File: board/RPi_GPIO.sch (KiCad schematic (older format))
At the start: 29 parts, among them IC1 ATMEGA328P-P, IC2 RFM69HW, J1 RPi_GPIO, P1 FTDI_CONN_01X06, P2 BATT_IN, P3 V_SRC_JPR, P4 UART_SRC_JPR, P5 LED_CONN, P6 SW_CONN, P7 CONN_01X01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

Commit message: first draft of the HAT layout
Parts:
- C1: footprint (none) -> Capacitors_SMD:c_elec_4x4.5
- C2, C5, C6: footprint (none) -> Capacitors_SMD:C_0805_HandSoldering
- C3, C4: footprint (none) -> Capacitors_SMD:C_1206_HandSoldering
- C7, C8: footprint (none) -> Capacitors_SMD:C_0603_HandSoldering
- D1: footprint (none) -> LEDs:LED-1206
- I1: footprint (none) -> TO_SOT_Packages_SMD:SOT-223
- IC1: footprint DIL28 -> Housings_DIP:DIP-28_W7.62mm
- IC2: footprint (none) -> mysensors-kicad:RFM69HW_SMD_Handsoldering
- JPR1, P5, P6: footprint (none) -> Pin_Headers:Pin_Header_Straight_1x02
- P1: footprint (none) -> Pin_Headers:Pin_Header_Straight_1x06
- P2: footprint (none) -> Pin_Headers:Pin_Header_Angled_1x02
- P3: footprint (none) -> Pin_Headers:Pin_Header_Straight_1x03
- P4: footprint (none) -> Pin_Headers:Pin_Header_Straight_2x03
- P7: footprint (none) -> Pin_Headers:Pin_Header_Straight_1x01
- Q1: footprint (none) -> TO_SOT_Packages_SMD:SOT-23_Handsoldering
- R1, R2, R4, R5: footprint (none) -> Resistors_SMD:R_0805_HandSoldering
- R3: footprint (none) -> Resistors_SMD:R_0603_HandSoldering
- SW1: footprint (none) -> Buttons_Switches_ThroughHole:SW_PUSH
- Y1: footprint (none) -> Crystals_Oscillators_SMD:Q_49U3HMS
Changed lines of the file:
@@
 F 0 "P2" H 6100 2900 50  0000 C CNN
 F 1 "BATT_IN" V 6200 2750 50  0000 C CNN
-F 2 "" H 6100 2750 60  0000 C CNN
+F 2 "Pin_Headers:Pin_Header_Angled_1x02" H 6100 2750 60  0001 C CNN
 F 3 "" H 6100 2750 60  0000 C CNN
 	1    6100 2750
@@
 F 0 "IC1" H 1500 6950 40  0000 L BNN
 F 1 "ATMEGA328P-P" H 2650 4300 40  0000 L BNN
-F 2 "DIL28" H 2250 5700 30  0000 C CIN
+F 2 "Housings_DIP:DIP-28_W7.62mm" H 2250 5700 30  0000 C CIN
 F 3 "" H 2250 5700 60  0000 C CNN
 	1    2250 5700
@@
 F 0 "C5" V 3600 5900 50  0000 L CNN
 F 1 "0.1µF" V 3800 5950 50  0000 C CNN
-F 2 "" H 3700 5950 60  0000 C CNN
+F 2 "Capacitors_SMD:C_0805_HandSoldering" H 3700 5950 60  0001 C CNN
 F 3 "" H 3700 5950 60  0000 C CNN
 	1    3700 5950
@@
 F 0 "C6" H 1175 6350 50  0000 L CNN
 F 1 "0.1µF" H 1175 6150 50  0000 L CNN
-F 2 "" H 1188 6100 30  0000 C CNN
+F 2 "Capacitors_SMD:C_0805_HandSoldering" H 1188 6100 30  0001 C CNN
 F 3 "" H 1150 6250 60  0000 C CNN
 	1    1150 6250
@@
 F 0 "R1" H 7630 1470 50  0000 L CNN
 F 1 "10K" H 7630 1410 50  0000 L CNN
-F 2 "" H 7600 1450 60  0000 C CNN
+F 2 "Resistors_SMD:R_0805_HandSoldering" H 7600 1450 60  0001 C CNN
 F 3 "" H 7600 1450 60  0000 C CNN
 	1    7600 1450
@@
 F 0 "R2" H 8330 1470 50  0000 L CNN
 F 1 "10K" H 8330 1410 50  0000 L CNN
-F 2 "" H 8300 1450 60  0000 C CNN
+F 2 "Resistors_SMD:R_0805_HandSoldering" H 8300 1450 60  0001 C CNN
 F 3 "" H 8300 1450 60  0000 C CNN
 	1    8300 1450
@@
 F 0 "Q1" V 7900 1500 50  0000 R CNN
 F 1 "BSS138_GSD" V 8250 1800 50  0000 R CNN
-F 2 "" H 8200 1650 29  0000 C CNN
+F 2 "TO_SOT_Packages_SMD:SOT-23_Handsoldering" H 8200 1650 29  0001 C CNN
 F 3 "" H 8000 1550 60  0000 C CNN
 	1    8000 1550
@@
 F 0 "P3" V 10050 1500 50  0000 C CNN
 F 1 "V_SRC_JPR" V 10150 1250 50  0000 C CNN
-F 2 "" H 10050 1250 60  0000 C CNN
+F 2 "Pin_Headers:Pin_Header_Straight_1x03" H 10050 1250 60  0001 C CNN
 F 3 "" H 10050 1250 60  0000 C CNN
 	1    10050 1250
@@
 F 0 "P4" V 10050 2950 50  0000 C CNN
 F 1 "UART_SRC_JPR" H 10050 2500 50  0000 C CNN
-F 2 "" H 10050 1500 60  0000 C CNN
+F 2 "Pin_Headers:Pin_Header_Straight_2x03" H 10050 1500 60  0001 C CNN
 F 3 "" H 10050 1500 60  0000 C CNN
 	1    10050 2700
@@
 F 0 "I1" H 7400 2800 60  0000 C CNN
 F 1 "TC1108" H 7600 2350 60  0000 C CNN
-F 2 "" H 7500 2600 60  0000 C CNN
+F 2 "TO_SOT_Packages_SMD:SOT-223" H 7500 2600 60  0001 C CNN
 F 3 "" H 7500 2600 60  0000 C CNN
 	1    7600 2650
@@
 F 0 "C4" H 8160 2870 50  0000 L CNN
 F 1 "1µF" H 8160 2720 50  0000 L CNN
-F 2 "" H 8150 2800 60  0000 C CNN
+F 2 "Capacitors_SMD:C_1206_HandSoldering" H 8150 2800 60  0001 C CNN
 F 3 "" H 8150 2800 60  0000 C CNN
 	1    8150 2800
@@
 F 0 "C3" H 6810 2820 50  0000 L CNN
 F 1 "1µF" H 6810 2670 50  0000 L CNN
-F 2 "" H 6800 2750 60  0000 C CNN
+F 2 "Capacitors_SMD:C_1206_HandSoldering" H 6800 2750 60  0001 C CNN
 F 3 "" H 6800 2750 60  0000 C CNN
 	1    6800 2750
@@
 F 0 "Y1" H 4450 5250 50  0000 C CNN
 F 1 "16MHz" H 4450 5450 50  0000 C CNN
-F 2 "" H 4450 5350 60  0000 C CNN
+F 2 "Crystals_Oscillators_SMD:Q_49U3HMS" H 4450 5350 60  0001 C CNN
 F 3 "" H 4450 5350 60  0000 C CNN
 	1    4450 5350
@@
 F 0 "C7" V 4500 5150 50  0000 L CNN
 F 1 "22pF" V 4600 5150 50  0000 L CNN
-F 2 "" H 4700 5200 60  0000 C CNN
+F 2 "Capacitors_SMD:C_0603_HandSoldering" H 4700 5200 60  0001 C CNN
 F 3 "" H 4700 5200 60  0000 C CNN
 	1    4700 5200
@@
 F 0 "C8" V 4800 5450 50  0000 L CNN
 F 1 "22pF" V 4900 5400 50  0000 L CNN
-F 2 "" H 4700 5500 60  0000 C CNN
+F 2 "Capacitors_SMD:C_0603_HandSoldering" H 4700 5500 60  0001 C CNN
 F 3 "" H 4700 5500 60  0000 C CNN
 	1    4700 5500
@@
 F 0 "R5" V 3800 5600 50  0000 L CNN
 F 1 "10K" V 3600 5600 50  0000 L CNN
-F 2 "" H 3700 5650 60  0000 C CNN
+F 2 "Resistors_SMD:R_0805_HandSoldering" H 3700 5650 60  0001 C CNN
 F 3 "" H 3700 5650 60  0000 C CNN
 	1    3700 5650
@@
 F 0 "C1" H 4460 2670 50  0000 L CNN
 F 1 "10µF" H 4460 2520 50  0000 L CNN
-F 2 "" H 4450 2600 60  0000 C CNN
+F 2 "Capacitors_SMD:c_elec_4x4.5" H 4450 2600 60  0001 C CNN
 F 3 "" H 4450 2600 60  0000 C CNN
 	1    4450 2600
@@
 F 0 "C2" H 4810 2670 50  0000 L CNN
 F 1 "0.1µF" H 4810 2520 50  0000 L CNN
-F 2 "" H 4800 2600 60  0000 C CNN
+F 2 "Capacitors_SMD:C_0805_HandSoldering" H 4800 2600 60  0001 C CNN
 F 3 "" H 4800 2600 60  0000 C CNN
 	1    4800 2600
@@
 F 0 "D1" V 6800 4500 50  0000 L CNN
 F 1 "SMD_LED" V 6650 4750 50  0000 R CNN
-F 2 "" V 6750 4400 60  0000 C CNN
+F 2 "LEDs:LED-1206" V 6750 4400 60  0001 C CNN
 F 3 "" V 6750 4400 60  0000 C CNN
 	1    6750 4400
@@
 F 0 "R3" H 6600 4150 50  0000 L CNN
 F 1 "560R" H 6500 4050 50  0000 L CNN
-F 2 "" H 6750 4100 60  0000 C CNN
+F 2 "Resistors_SMD:R_0603_HandSoldering" H 6750 4100 60  0001 C CNN
 F 3 "" H 6750 4100 60  0000 C CNN
 	1    6750 4100
@@
 F 0 "P5" H 7300 3850 50  0000 C CNN
 F 1 "LED_CONN" V 7400 3700 50  0000 C CNN
-F 2 "" H 7300 3700 60  0000 C CNN
+F 2 "Pin_Headers:Pin_Header_Straight_1x02" H 7300 3700 60  0001 C CNN
 F 3 "" H 7300 3700 60  0000 C CNN
 	1    7300 3700
@@
 F 0 "P1" H 6050 1750 50  0000 C CNN
 F 1 "FTDI_CONN_01X06" V 6250 1400 50  0000 C CNN
-F 2 "" H 6050 1400 60  0000 C CNN
+F 2 "Pin_Headers:Pin_Header_Straight_1x06" H 6050 1400 60  0001 C CNN
 F 3 "" H 6050 1400 60  0000 C CNN
 	1    6050 1400
@@
 F 0 "P6" H 7250 6000 50  0000 C CNN
 F 1 "SW_CONN" V 7350 5850 50  0000 C CNN
-F 2 "" H 7250 5850 60  0000 C CNN
+F 2 "Pin_Headers:Pin_Header_Straight_1x02" H 7250 5850 60  0001 C CNN
 F 3 "" H 7250 5850 60  0000 C CNN
 	1    7250 5850
@@
 F 0 "R4" H 6480 5620 50  0000 L CNN
 F 1 "10K" H 6480 5560 50  0000 L CNN
-F 2 "" H 6450 5600 60  0000 C CNN
+F 2 "Resistors_SMD:R_0805_HandSoldering" H 6450 5600 60  0001 C CNN
 F 3 "" H 6450 5600 60  0000 C CNN
 	1    6450 5600
@@
 F 0 "SW1" H 6600 5900 30  0000 C CNN
 F 1 "SWITCH" H 6600 5850 30  0000 C CNN
-F 2 "" H 6750 5900 60  0000 C CNN
+F 2 "Buttons_Switches_ThroughHole:SW_PUSH" H 6750 5900 60  0001 C CNN
 F 3 "" H 6750 5900 60  0000 C CNN
 	1    6750 5900
@@
 F 0 "IC2" H 9050 4700 60  0000 C CNN
 F 1 "RFM69HW" H 9500 3350 60  0000 C CNN
-F 2 "" H 9350 4550 60  0000 C CNN
+F 2 "mysensors-kicad:RFM69HW_SMD_Handsoldering" H 9350 4550 60  0001 C CNN
 F 3 "" H 9350 4550 60  0000 C CNN
 	1    9350 4550
@@
 F 0 "P7" H 10450 5550 50  0000 C CNN
 F 1 "CONN_01X01" V 10550 5450 50  0000 C CNN
-F 2 "" H 10450 5450 60  0000 C CNN
+F 2 "Pin_Headers:Pin_Header_Straight_1x01" H 10450 5450 60  0001 C CNN
 F 3 "" H 10450 5450 60  0000 C CNN
 	1    10450 5450
@@
 F 0 "JPR1" H 6750 3850 50  0000 C CNN
 F 1 "NC_JPR" H 6800 3950 50  0000 C CNN
-F 2 "" H 6550 3850 60  0000 C CNN
+F 2 "Pin_Headers:Pin_Header_Straight_1x02" H 6550 3850 60  0001 C CNN
 F 3 "" H 6550 3850 60  0000 C CNN
 	1    6550 3850

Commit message: changed LED resistor to 75ohms (0603 package)
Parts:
- R3: value 560R -> 75R
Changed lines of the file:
@@
 P 6750 4100
 F 0 "R3" H 6600 4150 50  0000 L CNN
-F 1 "560R" H 6500 4050 50  0000 L CNN
+F 1 "75R" H 6550 4050 50  0000 L CNN
 F 2 "Resistors_SMD:R_0603_HandSoldering" H 6750 4100 60  0001 C CNN
 F 3 "" H 6750 4100 60  0000 C CNN

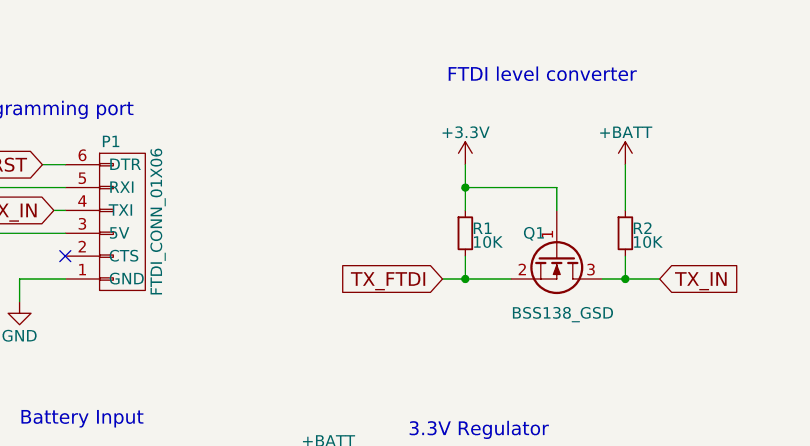
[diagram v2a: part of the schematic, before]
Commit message: fixed 3.3v error, and button rotation bug
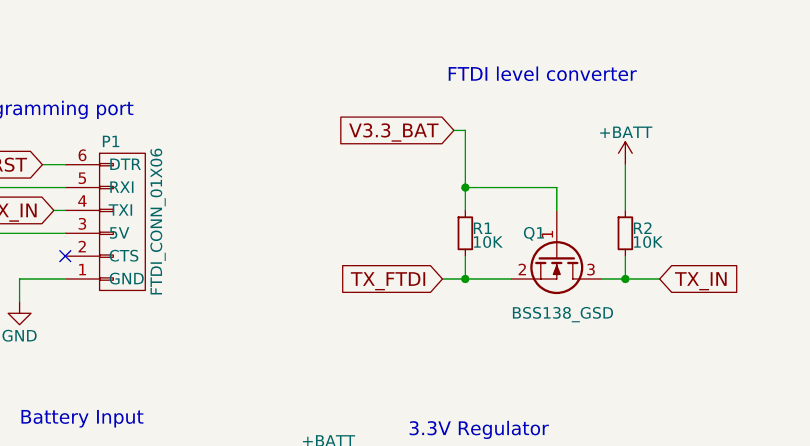
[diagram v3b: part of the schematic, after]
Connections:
- wire segments 146 -> 147
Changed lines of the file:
@@
 LIBS:contrib
 LIBS:valves
-LIBS:RPi_Hat-cache
 EELAYER 25 0
 EELAYER END
@@
 	1    0    0    -1
 $EndComp
-$Comp
-L +3.3V #PWR010
-U 1 1 560D442F
-P 7600 1150
-F 0 "#PWR010" H 7600 1000 50  0001 C CNN
-F 1 "+3.3V" H 7600 1290 50  0000 C CNN
-F 2 "" H 7600 1150 60  0000 C CNN
-F 3 "" H 7600 1150 60  0000 C CNN
-	1    7600 1150
-	1    0    0    -1
-$EndComp
 Text GLabel 7500 1650 0    60   Input ~ 0
 TX_FTDI
@@
 $EndComp
 $Comp
-L GND #PWR011
+L GND #PWR010
 U 1 1 560D5F6B
 P 7000 3000
-F 0 "#PWR011" H 7000 2750 50  0001 C CNN
+F 0 "#PWR010" H 7000 2750 50  0001 C CNN
 F 1 "GND" H 7000 2850 50  0000 C CNN
 F 2 "" H 7000 3000 60  0000 C CNN
@@
 $EndComp
 $Comp
-L +BATT #PWR012
+L +BATT #PWR011
 U 1 1 560D5F97
 P 7000 2500
-F 0 "#PWR012" H 7000 2350 50  0001 C CNN
+F 0 "#PWR011" H 7000 2350 50  0001 C CNN
 F 1 "+BATT" H 7000 2640 50  0000 C CNN
 F 2 "" H 7000 2500 60  0000 C CNN
@@
 V3.3_BAT
 $Comp
-L GND #PWR013
+L GND #PWR012
 U 1 1 560D60E0
 P 8150 3000
-F 0 "#PWR013" H 8150 2750 50  0001 C CNN
+F 0 "#PWR012" H 8150 2750 50  0001 C CNN
 F 1 "GND" H 8150 2850 50  0000 C CNN
 F 2 "" H 8150 3000 60  0000 C CNN
@@
 Connection ~ 8300 1650
 Wire Wire Line
-	7600 1150 7600 1350
+	7600 1000 7600 1350
 Wire Wire Line
 	7500 1650 7800 1650
@@
 Connection ~ 4450 5500
 $Comp
-L GND #PWR014
+L GND #PWR013
 U 1 1 560D7358
 P 4950 5600
-F 0 "#PWR014" H 4950 5350 50  0001 C CNN
+F 0 "#PWR013" H 4950 5350 50  0001 C CNN
 F 1 "GND" H 4950 5450 50  0000 C CNN
 F 2 "" H 4950 5600 60  0000 C CNN
@@
 V3.3
 $Comp
-L GND #PWR015
+L GND #PWR014
 U 1 1 560D8565
 P 4800 2900
-F 0 "#PWR015" H 4800 2650 50  0001 C CNN
+F 0 "#PWR014" H 4800 2650 50  0001 C CNN
 F 1 "GND" H 4800 2750 50  0000 C CNN
 F 2 "" H 4800 2900 60  0000 C CNN
@@
 $EndComp
 $Comp
-L GND #PWR016
+L GND #PWR015
 U 1 1 560DA177
 P 6750 4700
-F 0 "#PWR016" H 6750 4450 50  0001 C CNN
+F 0 "#PWR015" H 6750 4450 50  0001 C CNN
 F 1 "GND" H 6750 4550 50  0000 C CNN
 F 2 "" H 6750 4700 60  0000 C CNN
@@
 $EndComp
 $Comp
-L GND #PWR017
+L GND #PWR016
 U 1 1 560DB627
 P 7000 6050
-F 0 "#PWR017" H 7000 5800 50  0001 C CNN
+F 0 "#PWR016" H 7000 5800 50  0001 C CNN
 F 1 "GND" H 7000 5900 50  0000 C CNN
 F 2 "" H 7000 6050 60  0000 C CNN
@@
 	9850 5450 10250 5450
 $Comp
-L GND #PWR018
+L GND #PWR017
 U 1 1 560DCDCC
 P 10050 5800
-F 0 "#PWR018" H 10050 5550 50  0001 C CNN
+F 0 "#PWR017" H 10050 5550 50  0001 C CNN
 F 1 "GND" H 10050 5650 50  0000 C CNN
 F 2 "" H 10050 5800 60  0000 C CNN
@@
 Wire Wire Line
 	6750 3900 6750 4000
+Text GLabel 7550 1000 0    60   Input ~ 0
+V3.3_BAT
+Wire Wire Line
+	7600 1000 7550 1000
 $EndSCHEMATC

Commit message: Revert "up to date with remote"
This reverts commit 92056238b58dd1545c72053bc3b2b9ea0aa8e0b0.
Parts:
- removed C7, C8: 22pF, Capacitors_SMD:C_0603_HandSoldering, symbol C_Small
- removed IC1: ATMEGA328P-P, Housings_DIP:DIP-28_W7.62mm, symbol ATMEGA328P-P
- removed P4: UART_SRC_JPR, Pin_Headers:Pin_Header_Straight_2x03, symbol CONN_02X03
- removed Y1: 16MHz, Crystals_Oscillators_SMD:Q_49U3HMS, symbol Crystal_Small
- added IC1: ATMEGA328-A, local:TQFP-32_7x7mm_Pitch0.8mm, symbol ATMEGA328-A
- added P13: ICSP, local:ISCP_header, symbol CONN_02X03
- added P2: D8, local:Pin_Header_Straight_1x03, symbol CONN_01X03
- added P4: A1, local:Pin_Header_Straight_1x03, symbol CONN_01X03
- added P5: A2, local:Pin_Header_Straight_1x03, symbol CONN_01X03
- added P6: A3, local:Pin_Header_Straight_1x03, symbol CONN_01X03
- added P7: A4, local:Pin_Header_Straight_1x03, symbol CONN_01X03
- added P8: A5, local:Pin_Header_Straight_1x03, symbol CONN_01X03
- added R10, R6, R7, R8, R9: 10K, Resistors_SMD:R_0603_HandSoldering, symbol R_Small
- added SW2: RESET, local:KSEx00G_SW, symbol SW_PUSH_SMALL
- added SW3: SWITCH_4PDT, cloudmaker:SWITCH_4PDT_MFS401N, symbol SWITCH_4PDT
- added SW4: SWITCH_4DIP_SPST, local:SW_DIP_04_GULL_BINARY, symbol SWITCH_4DIP_SPST
- added Y1: RESONATOR, local:Resonator_3.2x1.3, symbol RESONATOR
- C1: footprint Capacitors_SMD:c_elec_4x4.5 -> local:c_elec_3x5.3
- D1: footprint LEDs:LED-1206 -> LEDs:LED_1206
- I1: footprint TO_SOT_Packages_SMD:SOT-223 -> TO_SOT_Packages_SMD:SOT-23_Handsoldering
- IC2: footprint mysensors-kicad:RFM69HW_SMD_Handsoldering -> local:RFM69
- J1: footprint RPi_Hat:Samtec_HLE-120-02-XXX-DV-BE-XX-XX -> cloudmaker:Samtec_HLE-120-02-XXX-DV-BE-XX-XX
- JPR1: footprint Pin_Headers:Pin_Header_Straight_1x02 -> local:NC_SMD_JPR
- P11: renamed from P2; footprint Pin_Headers:Pin_Header_Angled_1x02 -> local:bornier2
- P3: value V_SRC_JPR -> A0; footprint Pin_Headers:Pin_Header_Straight_1x03 -> local:Pin_Header_Straight_1x03
- R1, R2, R4, R5: footprint Resistors_SMD:R_0805_HandSoldering -> Resistors_SMD:R_0603_HandSoldering
- SW1: footprint Buttons_Switches_ThroughHole:SW_PUSH -> local:KSEx00G_SW
- renumbered P6 to P10, P7 to P12, P5 to P9
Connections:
- net labels added: ADC0, ADC1, ADC2, ADC3, ADC4, ADC5, NODE_ID_1, NODE_ID_2, NODE_ID_4, NODE_ID_8, NODE_ID_M, TEMP_D8
- wire segments 147 -> 205
- no-connect marks 46 -> 36
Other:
- note added: "A0-A5 ports"
- note added: "Binary node id selection"
- note added: "D8 port"
- note added: "ICSP header"
- note added: "Source selection switch"
- note removed: "Source Jumpers"
- moved on the sheet: C1, C2, C3, C4, C5, C6, D1, I1, IC2, J1, JPR1, P1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

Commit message: up to date with remote
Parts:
- removed IC1: ATMEGA328-A, local:TQFP-32_7x7mm_Pitch0.8mm, symbol ATMEGA328-A
- removed P13: ICSP, local:ISCP_header, symbol CONN_02X03
- removed P2: D8, local:Pin_Header_Straight_1x03, symbol CONN_01X03
- removed P4: A1, local:Pin_Header_Straight_1x03, symbol CONN_01X03
- removed P5: A2, local:Pin_Header_Straight_1x03, symbol CONN_01X03
- removed P6: A3, local:Pin_Header_Straight_1x03, symbol CONN_01X03
- removed P7: A4, local:Pin_Header_Straight_1x03, symbol CONN_01X03
- removed P8: A5, local:Pin_Header_Straight_1x03, symbol CONN_01X03
- removed R10, R6, R7, R8, R9: 10K, Resistors_SMD:R_0603_HandSoldering, symbol R_Small
- removed SW2: RESET, local:KSEx00G_SW, symbol SW_PUSH_SMALL
- removed SW3: SWITCH_4PDT, cloudmaker:SWITCH_4PDT_MFS401N, symbol SWITCH_4PDT
- removed SW4: SWITCH_4DIP_SPST, local:SW_DIP_04_GULL_BINARY, symbol SWITCH_4DIP_SPST
- removed Y1: RESONATOR, local:Resonator_3.2x1.3, symbol RESONATOR
- added C7, C8: 22pF, Capacitors_SMD:C_0603_HandSoldering, symbol C_Small
- added IC1: ATMEGA328P-P, Housings_DIP:DIP-28_W7.62mm, symbol ATMEGA328P-P
- added P4: UART_SRC_JPR, Pin_Headers:Pin_Header_Straight_2x03, symbol CONN_02X03
- added Y1: 16MHz, Crystals_Oscillators_SMD:Q_49U3HMS, symbol Crystal_Small
- C1: footprint local:c_elec_3x5.3 -> Capacitors_SMD:c_elec_4x4.5
- D1: footprint LEDs:LED_1206 -> LEDs:LED-1206
- I1: footprint TO_SOT_Packages_SMD:SOT-23_Handsoldering -> TO_SOT_Packages_SMD:SOT-223
- IC2: footprint local:RFM69 -> mysensors-kicad:RFM69HW_SMD_Handsoldering
- J1: footprint cloudmaker:Samtec_HLE-120-02-XXX-DV-BE-XX-XX -> RPi_Hat:Samtec_HLE-120-02-XXX-DV-BE-XX-XX
- JPR1: footprint local:NC_SMD_JPR -> Pin_Headers:Pin_Header_Straight_1x02
- P2: renamed from P11; footprint local:bornier2 -> Pin_Headers:Pin_Header_Angled_1x02
- P3: value A0 -> V_SRC_JPR; footprint local:Pin_Header_Straight_1x03 -> Pin_Headers:Pin_Header_Straight_1x03
- R1, R2, R4, R5: footprint Resistors_SMD:R_0603_HandSoldering -> Resistors_SMD:R_0805_HandSoldering
- SW1: footprint local:KSEx00G_SW -> Buttons_Switches_ThroughHole:SW_PUSH
- renumbered P9 to P5, P10 to P6, P12 to P7
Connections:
- net labels removed: ADC0, ADC1, ADC2, ADC3, ADC4, ADC5, NODE_ID_1, NODE_ID_2, NODE_ID_4, NODE_ID_8, NODE_ID_M, TEMP_D8
- wire segments 205 -> 147
- no-connect marks 36 -> 46
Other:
- note added: "Source Jumpers"
- note removed: "A0-A5 ports"
- note removed: "Binary node id selection"
- note removed: "D8 port"
- note removed: "ICSP header"
- note removed: "Source selection switch"
- moved on the sheet: C1, C2, C3, C4, C5, C6, D1, I1, IC2, J1, JPR1, P1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

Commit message: resonator, analog input bank, source switch
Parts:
- removed C7, C8: 22pF, Capacitors_SMD:C_0603_HandSoldering, symbol C_Small
- removed IC1: ATMEGA328P-P, Housings_DIP:DIP-28_W7.62mm, symbol ATMEGA328P-P
- removed P4: UART_SRC_JPR, Pin_Headers:Pin_Header_Straight_2x03, symbol CONN_02X03
- removed Y1: 16MHz, Crystals_Oscillators_SMD:Q_49U3HMS, symbol Crystal_Small
- added IC1: ATMEGA328-A, TQFP32, symbol ATMEGA328-A
- added P2: D4, local:Pin_Header_Straight_1x03, symbol CONN_01X03
- added P4: ADC1, symbol CONN_01X03
- added P5: ADC2, symbol CONN_01X03
- added P6: ADC3, symbol CONN_01X03
- added P7: ADC4, symbol CONN_01X03
- added P8: ADC5, symbol CONN_01X03
- added R6: R_Small, symbol R_Small
- added SW2: RESET, Buttons_Switches_ThroughHole:SW_PUSH, symbol SW_PUSH_SMALL
- added SW3: SWITCH_4PDT, symbol SWITCH_4PDT
- added Y1: RESONATOR, local:Resonator_3.2x1.3, symbol RESONATOR
- IC2: footprint mysensors-kicad:RFM69HW_SMD_Handsoldering -> local:RFM69
- P11: renamed from P2; footprint Pin_Headers:Pin_Header_Angled_1x02 -> local:bornier2
- P3: value V_SRC_JPR -> ADC0; footprint Pin_Headers:Pin_Header_Straight_1x03 -> local:Pin_Header_Straight_1x03
- renumbered P6 to P10, P7 to P12, P5 to P9
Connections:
- net labels added: ADC0, ADC1, ADC2, ADC3, ADC4, ADC5, NODE_ID_1, NODE_ID_2, NODE_ID_4, NODE_ID_8, NODE_ID_M, TEMP_D4
- wire segments 147 -> 174
- no-connect marks 46 -> 36
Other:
- note added: "A0-A5 ports"
- note added: "Source selection switch"
- note removed: "Source Jumpers"
- moved on the sheet: C1, C2, C3, C4, C5, C6, D1, I1, IC2, J1, JPR1, P1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

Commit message: footprint and documentation for the 4PDT source selector switch
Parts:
- SW3: footprint (none) -> cloudmaker:SWITCH_4PDT_MFS401N; Description (none) -> 4-pole, double throw slide switch; MFP (none) -> MFS401N-2-Z; Notes (none) -> 1.5mm leads. Can be placed either way round; Source (none) -> Digikey only; supplier1_link (none) -> http://www.digikey.co.uk/product-detail/en/copal-electronic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; supplier1_name (none) -> DIGIKEY
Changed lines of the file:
@@
 F 0 "SW3" H 9850 2850 60  0000 C CNN
 F 1 "SWITCH_4PDT" H 10650 1300 60  0000 C CNN
-F 2 "" H 10400 2700 60  0000 C CNN
-F 3 "" H 10400 2700 60  0000 C CNN
+F 2 "cloudmaker:SWITCH_4PDT_MFS401N" H 10400 2700 60  0001 C CNN
+F 3 "http://www.nidec-copal-electronics.com/e/catalog/switch/mfs.pdf" H 10400 2700 60  0001 C CNN
+F 4 "~" H 10400 2700 60  0001 C CNN "Characteristics"
+F 5 "4-pole, double throw slide switch" H 10400 2700 60  0001 C CNN "Description"
+F 6 "~" H 10400 2700 60  0001 C CNN "Package ID"
+F 7 "Digikey only" H 10400 2700 60  0001 C CNN "Source"
+F 8 "~" H 10400 2700 60  0001 C CNN "Critical"
+F 9 "1.5mm leads. Can be placed either way round" H 10400 2700 60  0001 C CNN "Notes"
+F 10 "MFS401N-2-Z" H 10400 2700 60  0001 C CNN "MFP"
+F 11 "DIGIKEY" H 10400 2700 60  0001 C CNN "supplier1_name"
+F 12 "~" H 10400 2700 60  0001 C CNN "supplier2_name"
+F 13 "http://www.digikey.co.uk/product-detail/en/copal-electronics-inc/MFS401N-2-Z/563-1568-ND/5086558" H 10400 2700 60  0001 C CNN "supplier1_link"
+F 14 "~" H 10400 2700 60  0001 C CNN "supplier2_link"
+F 15 "~" H 10400 2700 60  0001 C CNN "MFN"
 	1    10400 2700
 	1    0    0    -1
